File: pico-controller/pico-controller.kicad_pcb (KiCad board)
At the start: 2 copper layers, 130 x 80 mm, 126 parts, among them J1 Conn_01x02_Male, J10 Conn_01x03_Male, J11 Conn_01x03_Male, J12 Conn_01x03_Male, J13 Conn_01x03_Male, J14 Conn_01x03_Male, J15 Conn_01x03_Male, J16 Conn_01x02_Male, J17 Conn_01x02_Male, J18 Conn_01x02_Male, J19 Conn_01x02_Male, J20 Conn_01x02_Male, J21 Conn_01x06_Male, J22 LCD I2C, J23 Conn_01x07_Male, J3 Conn_01x02_Male, J8 Conn_01x04_Male, J9 Conn_01x04_Male, Q1 BSS138, Q10 BSS138, Q11 BSS138, Q12 BSS138, Q13 BSS138, Q14 TIP122, Q15 BSS138, Q16 BSS138, Q17 BC817, Q18 BC817, Q2 BSS138, Q3 BSS138, Q4 BSS138, Q5 BSS138, Q6 BSS138, Q7 BSS138, Q8 BSS138, Q9 BSS138, SW1 SW_Push, U1 MCP3208, U2 LM4040DBZ-5.0, U3 24LC1025, U4 Pico, U5 IR2110, U6 IR2110

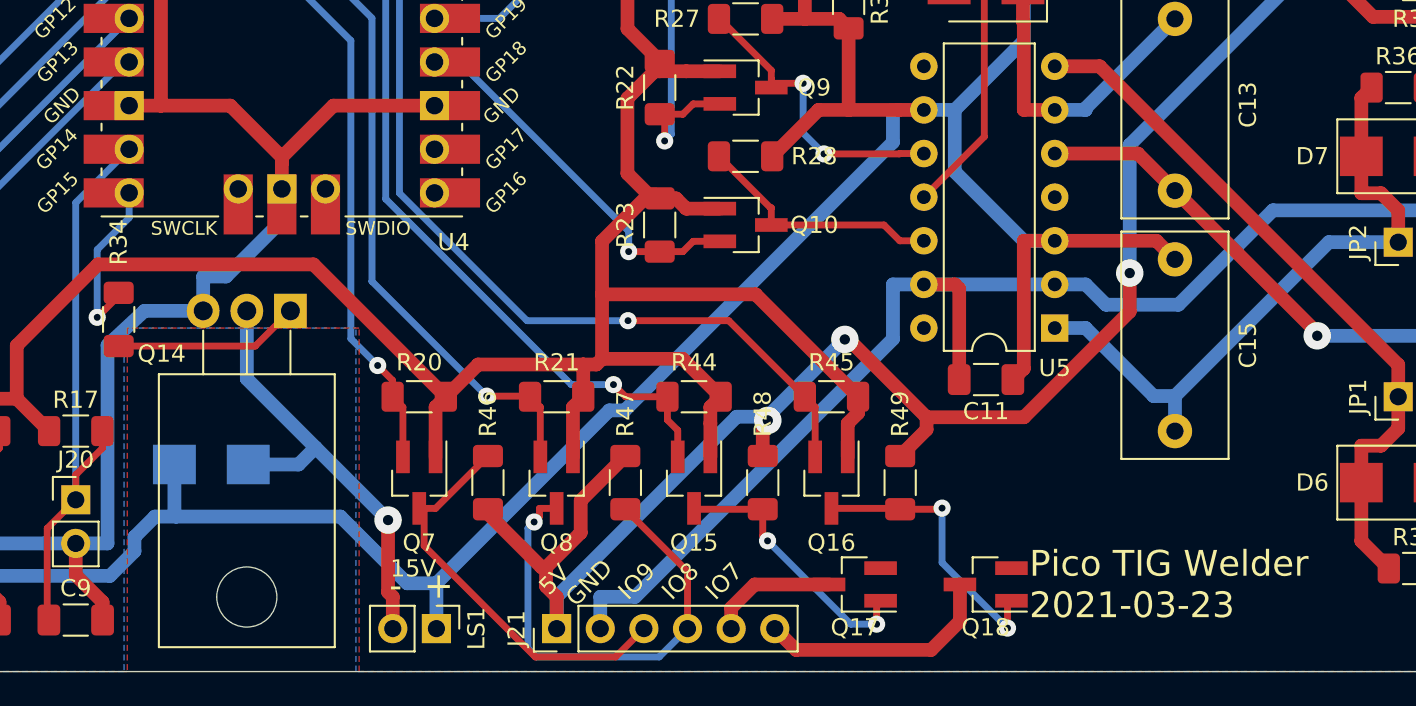
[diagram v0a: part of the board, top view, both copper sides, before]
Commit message: Reduced volatage of the speaker in the tig-welder controller board
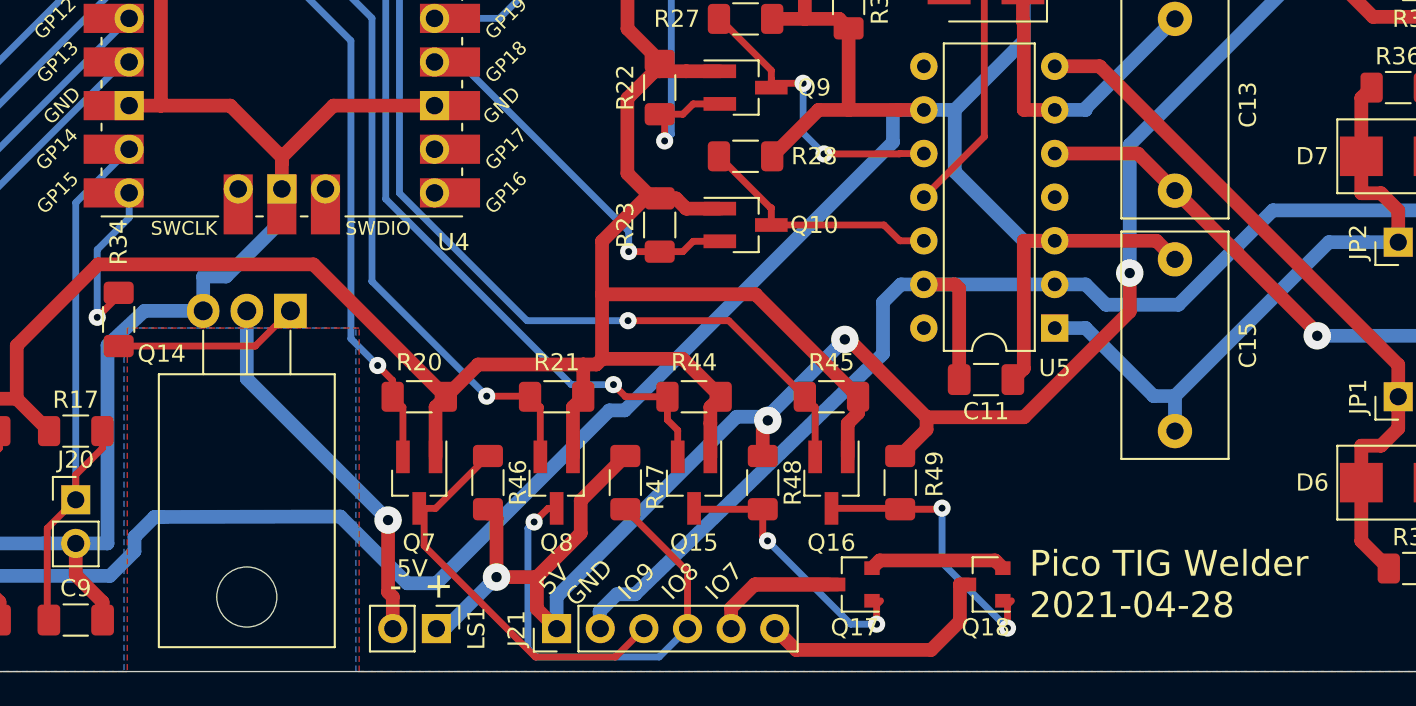
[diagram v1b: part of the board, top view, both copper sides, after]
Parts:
- removed D1: STTH212U, Diode_SMD:D_SMB
- Q17, Q18: footprint Package_TO_SOT_SMD:SOT-23_Handsoldering -> Package_TO_SOT_SMD:SOT-23
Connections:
- LS1 pad 1: +15V -> +5V
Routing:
- net GND: track 632.0 -> 639.3 mm
- net +5V: track 448.1 -> 455.1 mm, vias 7 -> 8
- net +15V: track 328.2 -> 322.5 mm
- net Net-(J21-Pad5): track 7.47 -> 12.3 mm
- net Net-(LS1-Pad2): track 26.3 -> 22.0 mm
- net Net-(J21-Pad6): track 14.1 -> 14.6 mm
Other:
- board text added: "Pico TIG Welder 2021-04-28"
- board text removed: "Pico TIG Welder 2021-03-23"
